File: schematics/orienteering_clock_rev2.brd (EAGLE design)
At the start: 100 x 81.3 mm, 67 parts, among them IC1 TPIC6B595N, IC2 TPIC6B595N, J2 ICSP, Q1 IRFU9024V, Q2 IRFU9024V, Q3 IRFU9024V, Q4 IRFU9024V, Q5 IRFU9024V, Q6 IRFU9024V, T1 BC547, Y1 16MHz

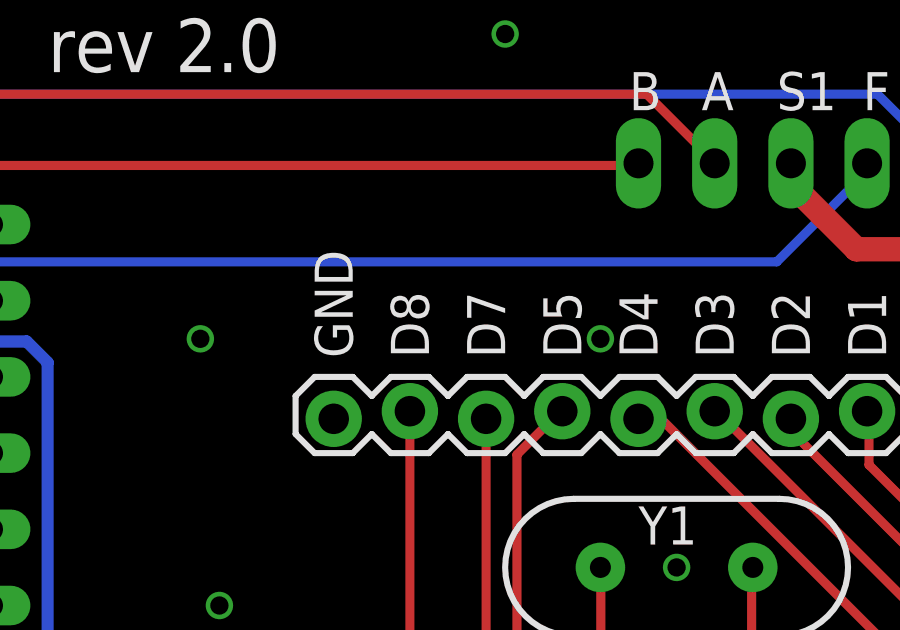
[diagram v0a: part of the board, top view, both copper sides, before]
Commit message: schematics: fix errors on silkscreen
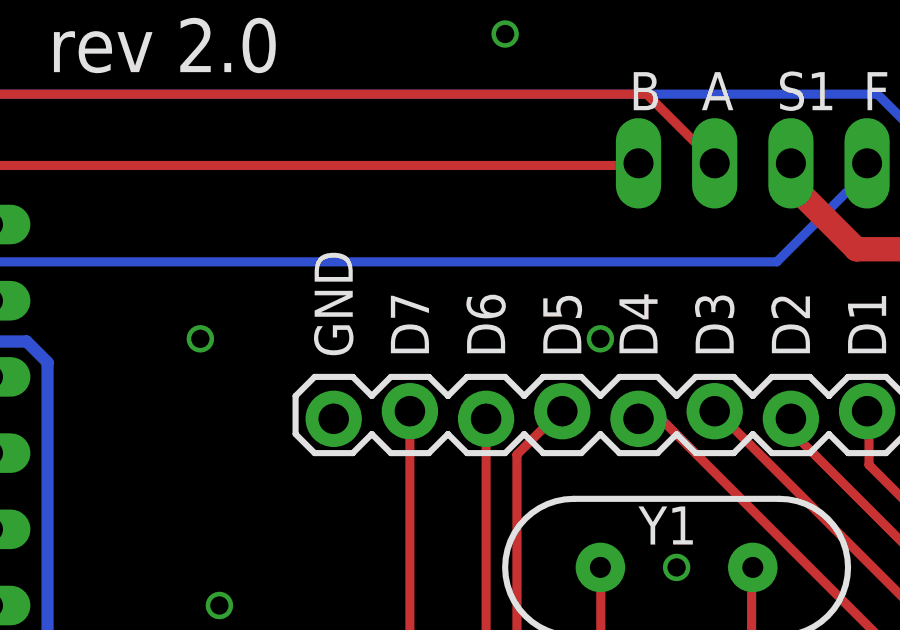
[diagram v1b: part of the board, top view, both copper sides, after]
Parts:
- C5: value 0.1uF -> 100 nF
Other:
- board text added: "D6"
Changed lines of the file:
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@@
 <text x="80.645" y="29.21" size="1.27" layer="25" font="vector" rot="R90">SCL</text>
 <text x="60.325" y="64.135" size="1.27" layer="25" font="vector" rot="R90">GND</text>
-<text x="62.865" y="64.135" size="1.27" layer="25" font="vector" rot="R90">D8</text>
-<text x="65.405" y="64.135" size="1.27" layer="25" font="vector" rot="R90">D7</text>
+<text x="62.865" y="64.135" size="1.27" layer="25" font="vector" rot="R90">D7</text>
+<text x="65.405" y="64.135" size="1.27" layer="25" font="vector" rot="R90">D6</text>
 <text x="67.945" y="64.135" size="1.27" layer="25" font="vector" rot="R90">D5</text>
 <text x="70.485" y="64.135" size="1.27" layer="25" font="vector" rot="R90">D4</text>
@@
 <attribute name="VALUE" x="74.295" y="52.324" size="0.4064" layer="27" rot="R180"/>
 </element>
-<element name="C5" library="SparkFun" package="CAP-PTH-SMALL" value="0.1uF" x="94.615" y="54.864" smashed="yes" rot="R270">
+<element name="C5" library="SparkFun" package="CAP-PTH-SMALL" value="100 nF" x="94.615" y="54.864" smashed="yes" rot="R270">
 <attribute name="NAME" x="94.107" y="51.308" size="0.4064" layer="25" rot="R270"/>
 <attribute name="VALUE" x="94.742" y="51.308" size="0.4064" layer="27" rot="R270"/>

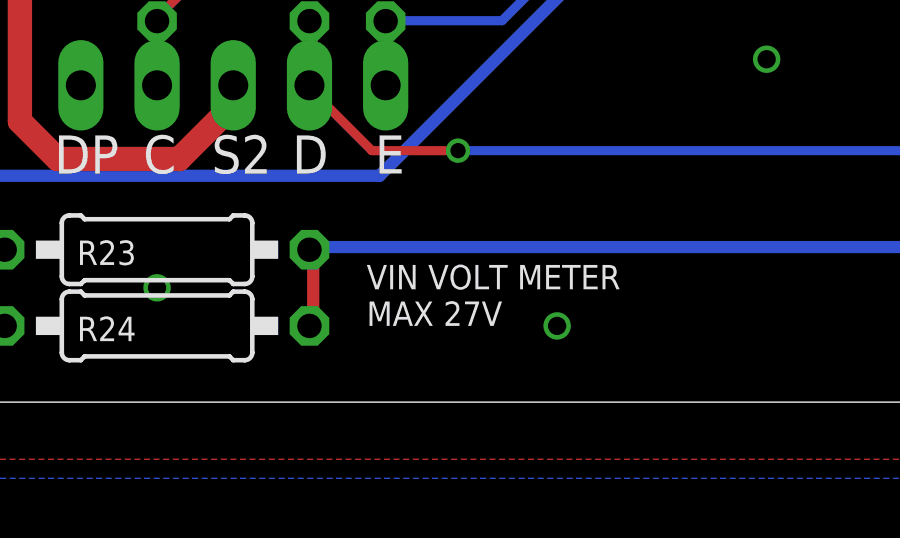
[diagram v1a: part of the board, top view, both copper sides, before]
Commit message: schematics: updated voltage sense, resistor values for new display
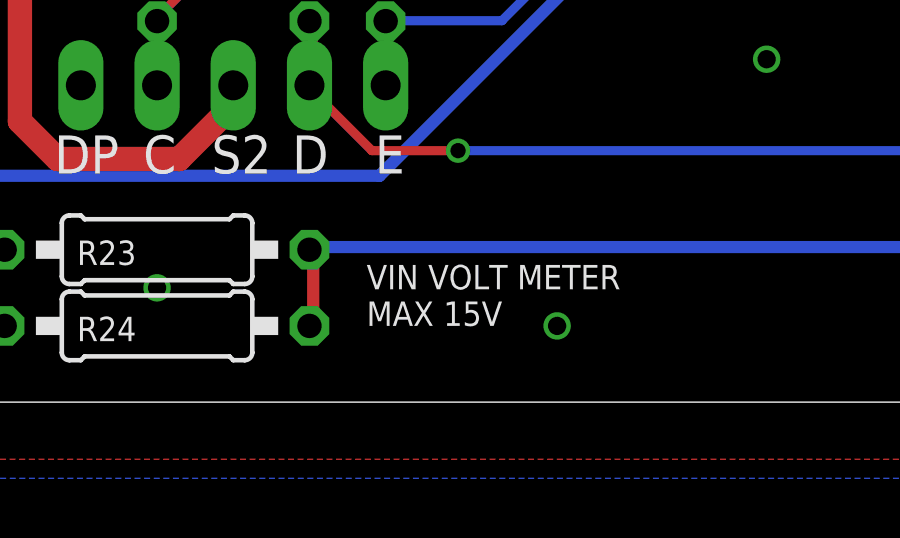
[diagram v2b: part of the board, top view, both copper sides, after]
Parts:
- R10, R11, R12, R13, R7, R8, R9: value 22R -> 47R
- R23: value 1M -> 10K
- R24: value 220k -> 4K7
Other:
- board text added: "VIN VOLT METER MAX 15V"
- board text removed: "VIN VOLT METER MAX 27V"
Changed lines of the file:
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@@
 <text x="5.334" y="7.239" size="0.8128" layer="25" font="vector">B-</text>
 <text x="31.115" y="2.54" size="0.8128" layer="21">VIN VOLT METER
-MAX 27V</text>
+MAX 15V</text>
 <text x="6.985" y="20.955" size="0.6096" layer="21">VIN 7 - 27V
 VDD 10 - 20V</text>
@@
 <attribute name="VALUE" x="10.287" y="39.37" size="0.8128" layer="27" ratio="10" rot="R180"/>
 </element>
-<element name="R10" library="resistor" package="0207/10" value="22R" x="11.43" y="63.5" smashed="yes" rot="R180">
+<element name="R10" library="resistor" package="0207/10" value="47R" x="11.43" y="63.5" smashed="yes" rot="R180">
 <attribute name="NAME" x="8.763" y="62.992" size="0.8128" layer="25" ratio="10" rot="R180" align="top-right"/>
 <attribute name="VALUE" x="12.0396" y="62.992" size="0.8128" layer="27" ratio="10" rot="R180" align="top-right"/>
 </element>
-<element name="R11" library="resistor" package="0207/10" value="22R" x="11.43" y="60.96" smashed="yes" rot="R180">
+<element name="R11" library="resistor" package="0207/10" value="47R" x="11.43" y="60.96" smashed="yes" rot="R180">
 <attribute name="NAME" x="8.763" y="60.452" size="0.8128" layer="25" ratio="10" rot="R180" align="top-right"/>
 <attribute name="VALUE" x="12.0396" y="60.452" size="0.8128" layer="27" ratio="10" rot="R180" align="top-right"/>
 </element>
-<element name="R12" library="resistor" package="0207/10" value="22R" x="11.43" y="58.42" smashed="yes" rot="R180">
+<element name="R12" library="resistor" package="0207/10" value="47R" x="11.43" y="58.42" smashed="yes" rot="R180">
 <attribute name="NAME" x="8.763" y="57.912" size="0.8128" layer="25" ratio="10" rot="R180" align="top-right"/>
 <attribute name="VALUE" x="12.0396" y="57.912" size="0.8128" layer="27" ratio="10" rot="R180" align="top-right"/>
 </element>
-<element name="R13" library="resistor" package="0207/10" value="22R" x="11.43" y="55.88" smashed="yes" rot="R180">
+<element name="R13" library="resistor" package="0207/10" value="47R" x="11.43" y="55.88" smashed="yes" rot="R180">
 <attribute name="NAME" x="8.763" y="55.372" size="0.8128" layer="25" ratio="10" rot="R180" align="top-right"/>
 <attribute name="VALUE" x="12.0396" y="55.372" size="0.8128" layer="27" ratio="10" rot="R180" align="top-right"/>
@@
 <attribute name="VALUE" x="93.091" y="57.8104" size="0.8128" layer="27" ratio="10" rot="R90"/>
 </element>
-<element name="R23" library="resistor" package="0207/10" value="1M" x="24.13" y="5.08" smashed="yes" rot="R180">
+<element name="R23" library="resistor" package="0207/10" value="10K" x="24.13" y="5.08" smashed="yes" rot="R180">
 <attribute name="NAME" x="21.463" y="4.572" size="0.8128" layer="25" ratio="10" rot="R180" align="top-right"/>
 <attribute name="VALUE" x="24.6126" y="4.572" size="0.8128" layer="27" ratio="10" rot="R180" align="top-right"/>
 </element>
-<element name="R24" library="resistor" package="0207/10" value="220k" x="24.13" y="2.54" smashed="yes">
+<element name="R24" library="resistor" package="0207/10" value="4K7" x="24.13" y="2.54" smashed="yes">
 <attribute name="NAME" x="21.463" y="2.032" size="0.8128" layer="25" ratio="10"/>
 <attribute name="VALUE" x="24.5364" y="2.032" size="0.8128" layer="27" ratio="10"/>
@@
 <attribute name="VALUE" x="19.177" y="30.48" size="0.8128" layer="27" ratio="10" rot="R180"/>
 </element>
-<element name="R7" library="resistor" package="0207/10" value="22R" x="11.43" y="71.12" smashed="yes" rot="R180">
+<element name="R7" library="resistor" package="0207/10" value="47R" x="11.43" y="71.12" smashed="yes" rot="R180">
 <attribute name="NAME" x="8.763" y="70.612" size="0.8128" layer="25" ratio="10" rot="R180" align="top-right"/>
 <attribute name="VALUE" x="12.0396" y="70.612" size="0.8128" layer="27" ratio="10" rot="R180" align="top-right"/>
 </element>
-<element name="R8" library="resistor" package="0207/10" value="22R" x="11.43" y="68.58" smashed="yes" rot="R180">
+<element name="R8" library="resistor" package="0207/10" value="47R" x="11.43" y="68.58" smashed="yes" rot="R180">
 <attribute name="NAME" x="8.763" y="68.072" size="0.8128" layer="25" ratio="10" rot="R180" align="top-right"/>
 <attribute name="VALUE" x="12.0396" y="68.072" size="0.8128" layer="27" ratio="10" rot="R180" align="top-right"/>
 </element>
-<element name="R9" library="resistor" package="0207/10" value="22R" x="11.43" y="66.04" smashed="yes" rot="R180">
+<element name="R9" library="resistor" package="0207/10" value="47R" x="11.43" y="66.04" smashed="yes" rot="R180">
 <attribute name="NAME" x="8.763" y="65.532" size="0.8128" layer="25" ratio="10" rot="R180" align="top-right"/>
 <attribute name="VALUE" x="12.0396" y="65.532" size="0.8128" layer="27" ratio="10" rot="R180" align="top-right"/>

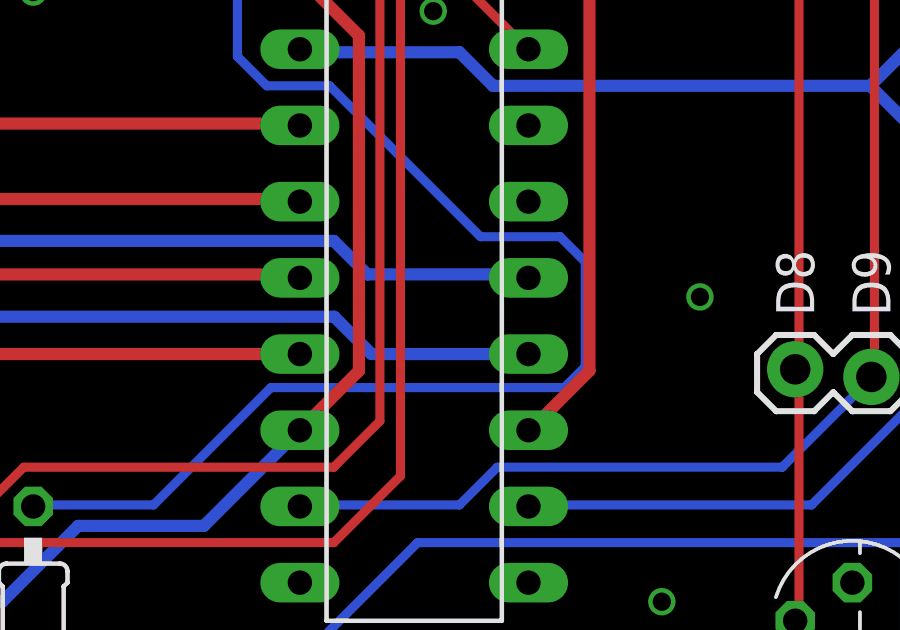
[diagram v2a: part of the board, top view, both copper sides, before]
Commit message: schematics: inverted small displays bug, revision 2.1
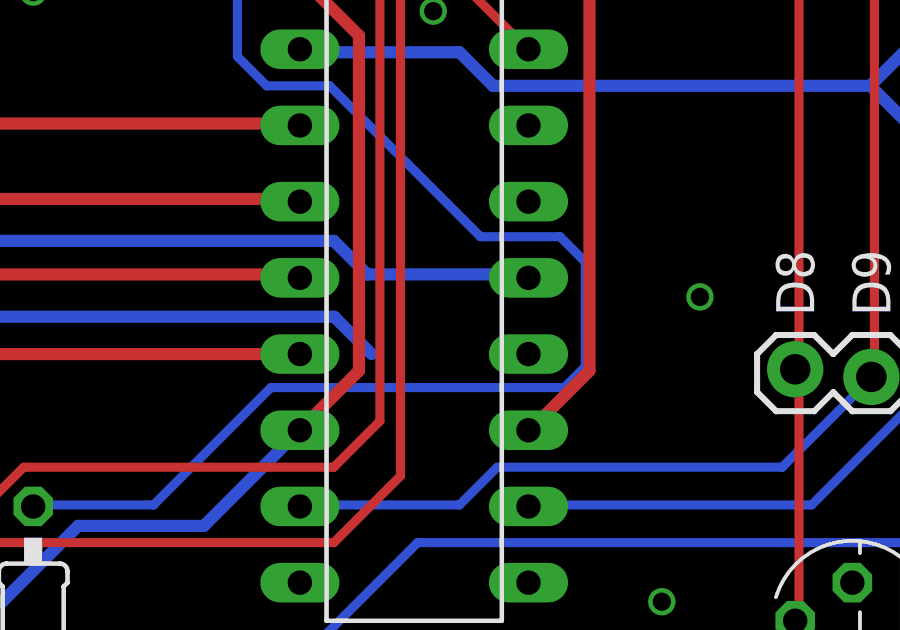
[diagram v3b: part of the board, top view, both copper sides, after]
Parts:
- R21: value 560R -> 220R
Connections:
- net S_1: now also IC2.14; no longer IC2.15
- net S_2: now also IC2.15; no longer IC2.14
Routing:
- net S_2: track 43.1 -> 37.9 mm
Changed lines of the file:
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@@
 <attribute name="VALUE" x="32.131" y="64.0334" size="0.8128" layer="27" ratio="10" rot="R90"/>
 </element>
-<element name="R21" library="resistor" package="0207/10" value="560R" x="11.43" y="53.34" smashed="yes" rot="R180">
+<element name="R21" library="resistor" package="0207/10" value="220R" x="11.43" y="53.34" smashed="yes" rot="R180">
 <attribute name="NAME" x="8.763" y="52.832" size="0.8128" layer="25" ratio="10" rot="R180" align="top-right"/>
 <attribute name="VALUE" x="11.6586" y="52.832" size="0.8128" layer="27" ratio="10" rot="R180" align="top-right"/>
@@
 </signal>
 <signal name="S_1">
-<contactref element="IC2" pad="15"/>
 <contactref element="Q5" pad="1"/>
 <contactref element="R6" pad="1"/>
@@
 <wire x1="22.7711" y1="31.7119" x2="41.7703" y2="31.7119" width="0.4064" layer="16"/>
 <wire x1="20.3962" y1="29.337" x2="22.7711" y2="31.7119" width="0.4064" layer="16"/>
-<wire x1="48.1965" y1="30.5943" x2="48.26" y2="30.48" width="0.3048" layer="16"/>
 <wire x1="20.3962" y1="29.337" x2="20.32" y2="29.21" width="0.3048" layer="16"/>
+<contactref element="IC2" pad="14"/>
+<wire x1="48.1965" y1="30.5943" x2="48.26" y2="27.94" width="0" layer="19" extent="16-16"/>
 </signal>
 <signal name="S_2">
-<contactref element="IC2" pad="14"/>
 <contactref element="Q6" pad="1"/>
 <contactref element="R5" pad="1"/>
@@
 <wire x1="11.3157" y1="29.1973" x2="11.43" y2="29.21" width="0.3048" layer="1"/>
 <wire x1="11.176" y1="26.6827" x2="11.176" y2="26.67" width="0.3048" layer="1"/>
-<wire x1="43.0276" y1="27.94" x2="48.26" y2="27.94" width="0.4064" layer="16"/>
 <wire x1="41.783" y1="29.1846" x2="43.0276" y2="27.94" width="0.4064" layer="16"/>
 <wire x1="24.9936" y1="29.1846" x2="41.783" y2="29.1846" width="0.4064" layer="16"/>
@@
 <wire x1="11.176" y1="26.543" x2="13.1318" y2="24.5872" width="0.4064" layer="16"/>
 <wire x1="11.176" y1="26.543" x2="11.176" y2="26.67" width="0.4064" layer="16"/>
+<contactref element="IC2" pad="15"/>
+<wire x1="43.0276" y1="27.94" x2="48.26" y2="30.48" width="0" layer="19" extent="16-16"/>
 </signal>
 <signal name="D0">

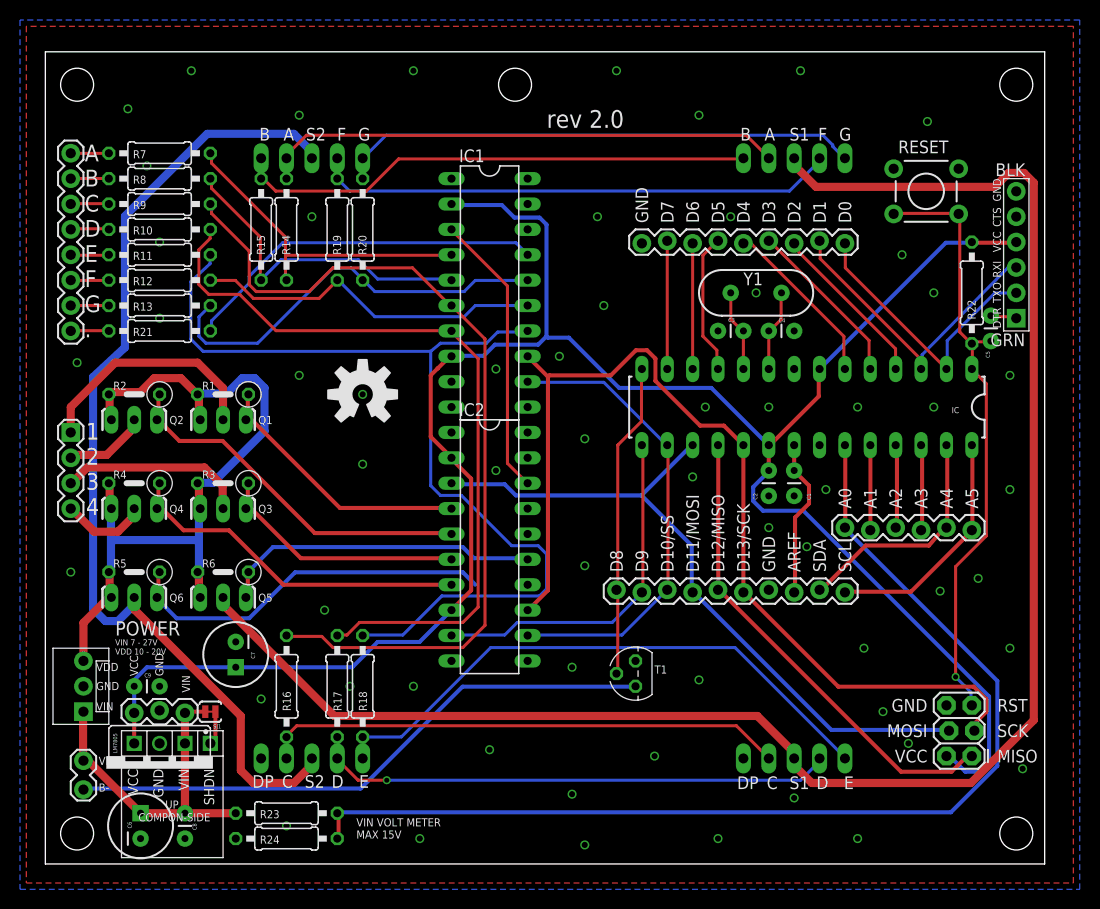
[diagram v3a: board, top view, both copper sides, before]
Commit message: schematics: add different assembly variants, small fixes
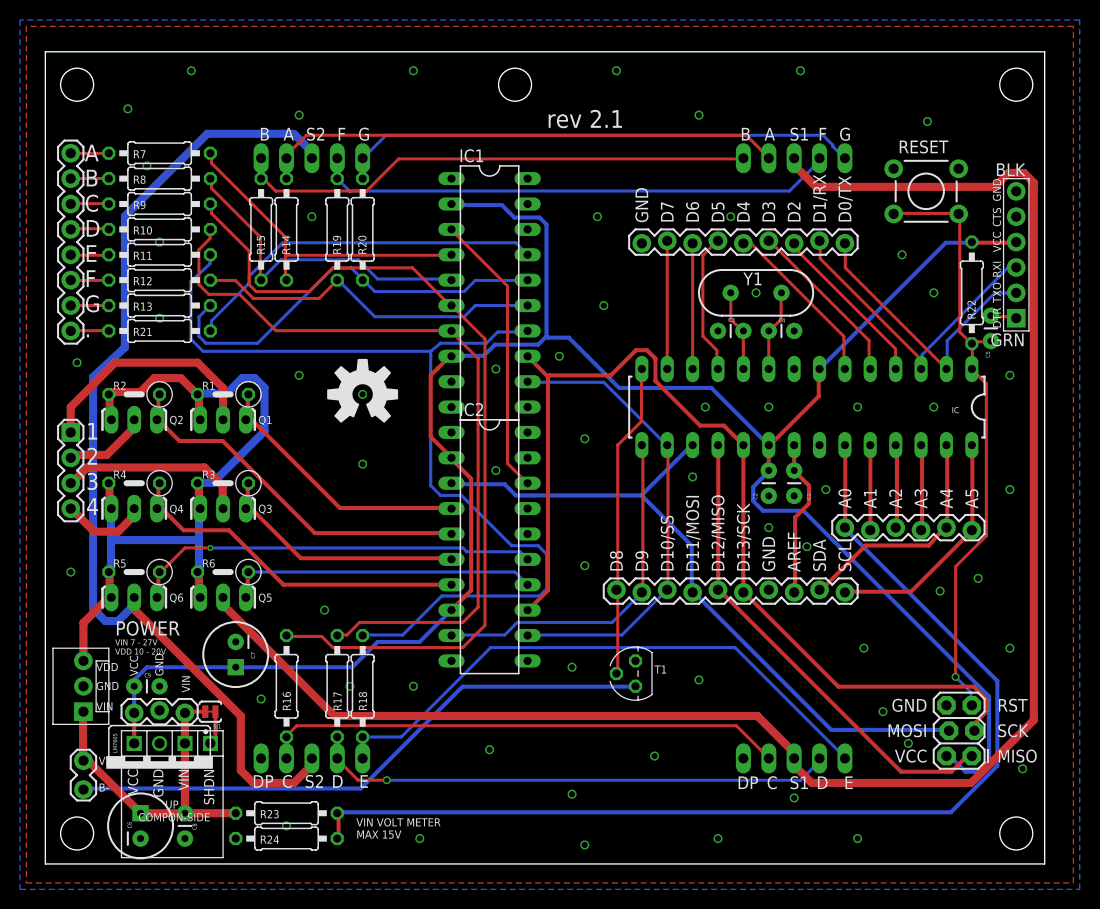
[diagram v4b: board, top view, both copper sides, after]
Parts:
- R10, R11, R12, R13, R7, R8, R9: value 47R -> 22R/1W
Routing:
- net S_2: track 37.9 -> 41.0 mm, vias 0 -> 1
- net S_1: track 32.1 -> 31.2 mm
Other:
- board text added: "D0/TX"
- board text added: "D1/RX"
- board text added: "For power you can either use POLOLU step-down buck converter or LM7805 with caps"
- board text added: "rev 2.1"
- board text removed: "D0"
- board text removed: "D1"
- board text removed: "For power you can either use POLOLU step-down buck converter or LM7085 with caps"
- board text removed: "rev 2.0"
